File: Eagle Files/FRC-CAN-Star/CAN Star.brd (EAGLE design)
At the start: 51.5 x 30.7 mm, 12 parts

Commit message: Updated Eagle Files
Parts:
- added JUMPER1, JUMPER2: (no value), SparkFun-Connectors:1X03
- moved CAN-R1 2.27 mm to (5.59, 17.5), turned to 186 degrees
- moved CAN-R2 2.27 mm to (45.9, 17.5), turned to 174 degrees
- moved CAN-0 1.27 mm to (5.41, 3.89)
- moved CAN-1 1.27 mm to (15.6, 3.89)
- moved CAN-2 1.27 mm to (25.7, 3.89)
- moved CAN-3 1.27 mm to (35.9, 3.89)
- moved CAN-4 1.27 mm to (46.1, 3.89)
- moved CAN-5 1.27 mm to (5.41, 26.8)
- moved CAN-6 1.27 mm to (15.6, 26.8)
- moved CAN-7 1.27 mm to (25.7, 26.8)
- moved CAN-8 1.27 mm to (35.9, 26.8)
- moved CAN-9 1.27 mm to (46.1, 26.8)
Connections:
- new net N$1: CAN-R1.1, JUMPER1.1
- new net N$2: CAN-R2.1, JUMPER2.1
- net CAN-A: now also JUMPER1.2, JUMPER2.2; no longer CAN-R1.1, CAN-R2.1
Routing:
- net CAN-A: track 125.6 -> 154.0 mm
- net CAN-B: track 125.6 -> 140.1 mm
- net N$1: track 0.00 -> 11.4 mm
- net N$2: track 0.00 -> 5.55 mm
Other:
- board size 51.5 x 30.7 mm -> 53.5 x 55.1 mm
- board text added: "G(L)"
- board text added: "ON"
- board text added: "Star Board v3"
- board text added: "Y(H)"
- board text removed: "Star Board v1"

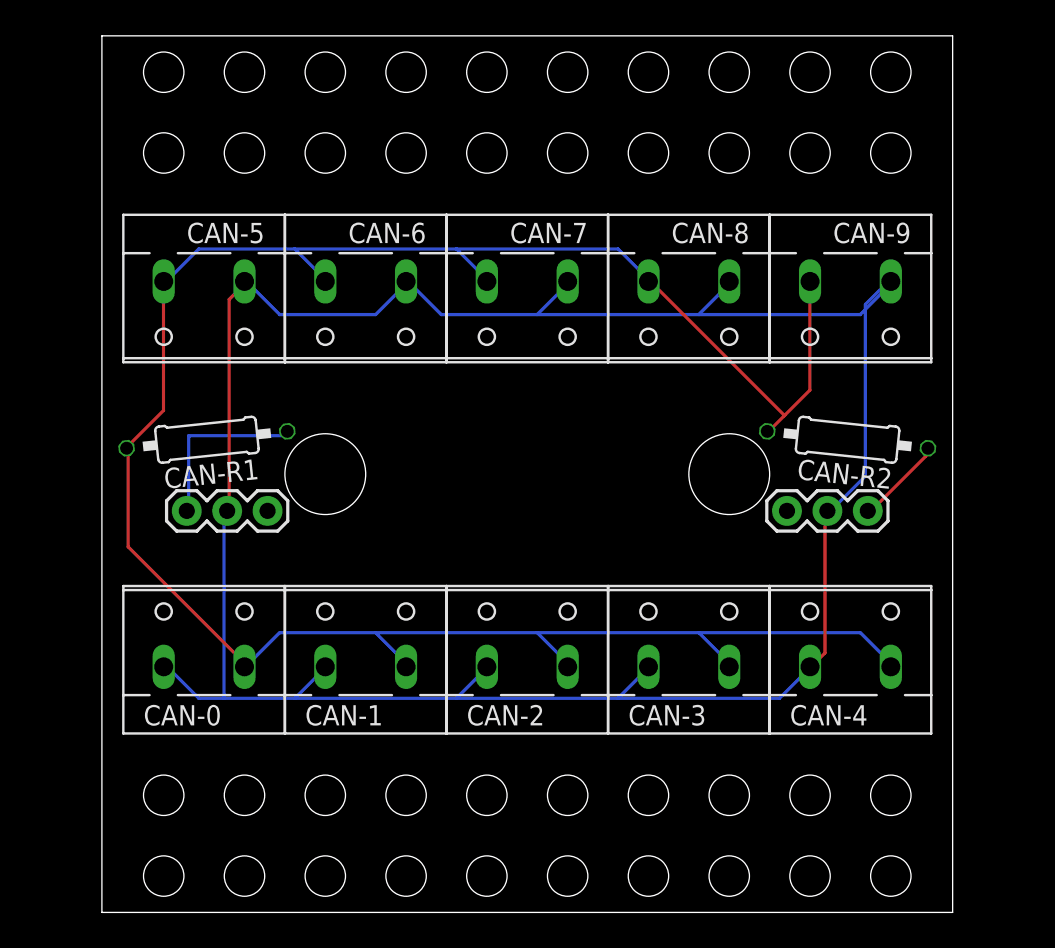
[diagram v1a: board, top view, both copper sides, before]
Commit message: Updated with strain relief holes, but not finalized yet.
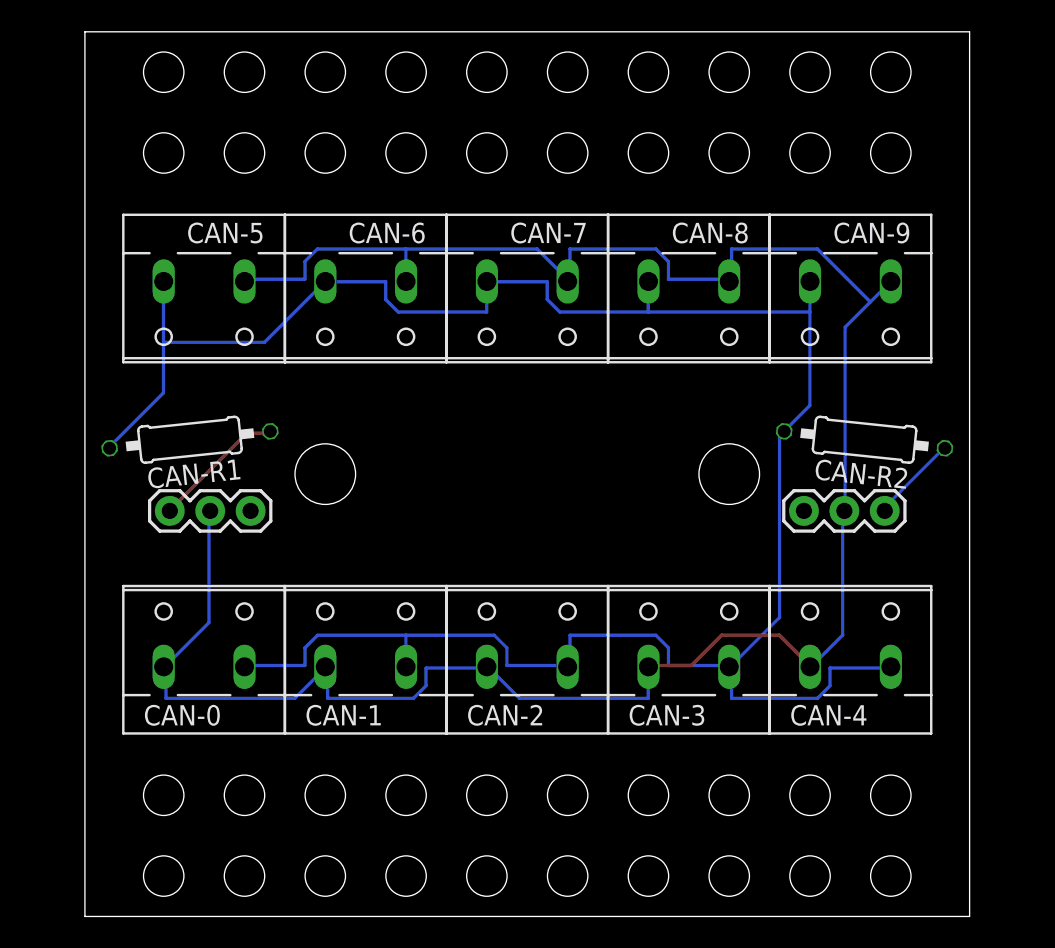
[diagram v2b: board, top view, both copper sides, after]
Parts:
- moved CAN-R2 1.07 mm to (46.9, 17.5)
- moved JUMPER1 1.07 mm to (3.25, 13.1)
- moved JUMPER2 1.07 mm to (48.2, 13.1)
- moved CAN-R1 1.07 mm to (4.52, 17.5)
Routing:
- net CAN-A: track 154.0 -> 139.4 mm
- net N$1: track 11.4 -> 8.44 mm
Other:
- board size 53.5 x 55.1 mm -> 55.6 x 55.6 mm
- board text added: "Star Board v4"
- board text removed: "Star Board v3"

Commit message: Finalized Star PCB
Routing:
- net CAN-A: track 139.4 -> 150.3 mm
- net CAN-B: track 139.7 -> 146.8 mm
- net N$1: track 8.44 -> 11.1 mm
- net N$2: track 5.53 -> 6.24 mm
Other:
- board size 55.6 x 55.6 mm -> 55.6 x 55.1 mm
- board text added: "Star Board v5"
- board text removed: "Star Board v4"

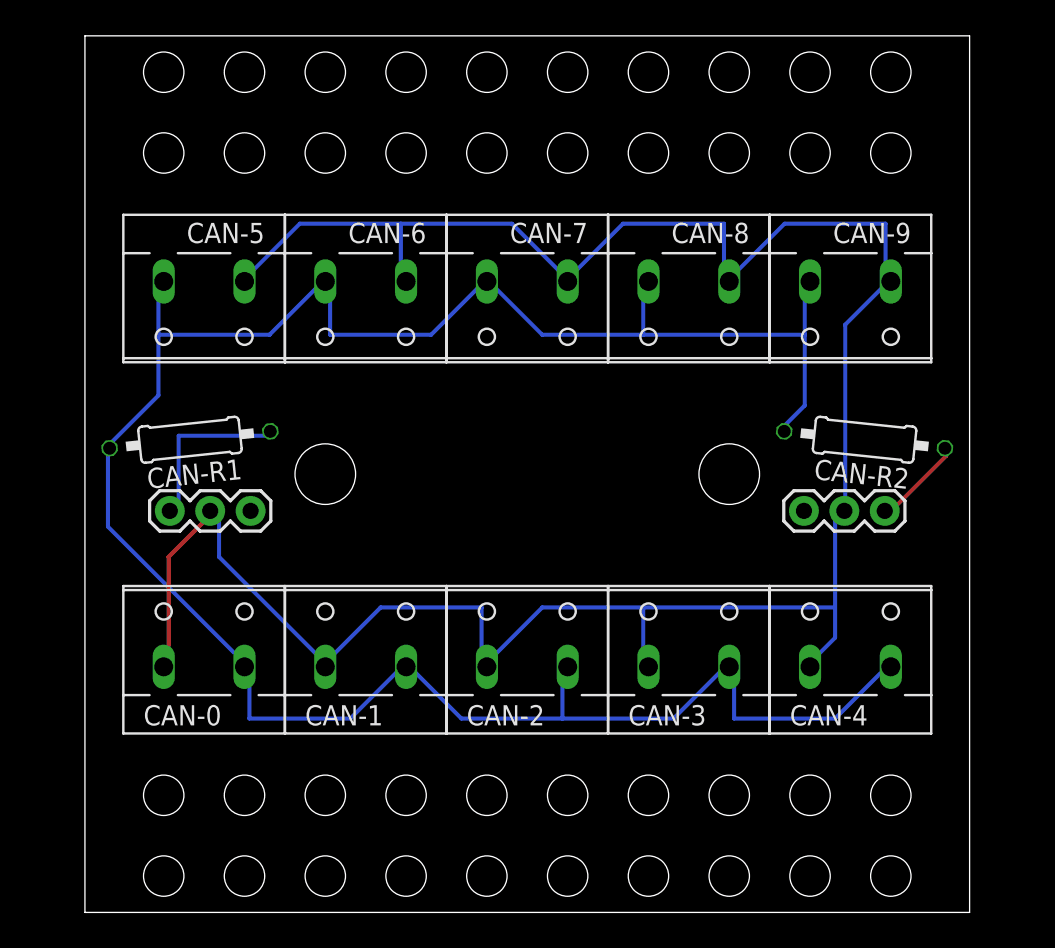
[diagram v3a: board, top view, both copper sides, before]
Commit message: Added additional mounting holes
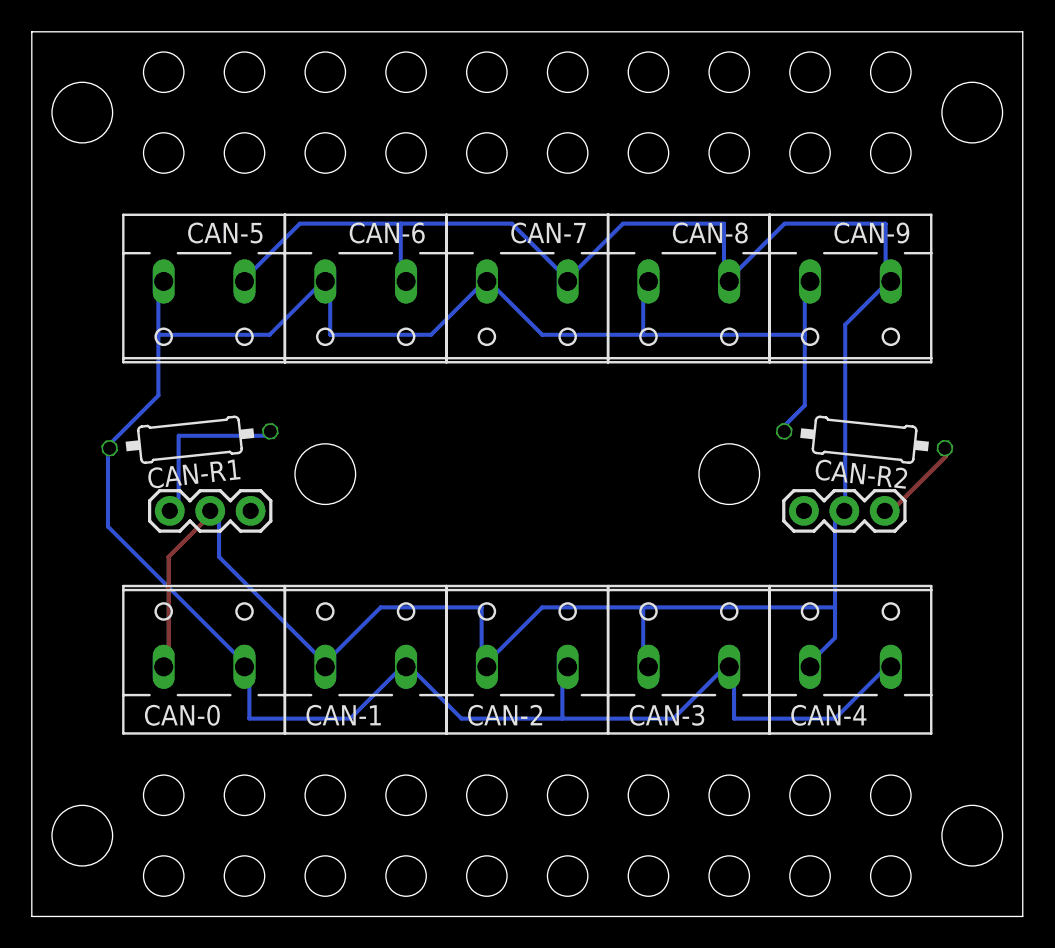
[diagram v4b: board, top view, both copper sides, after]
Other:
- board size 55.6 x 55.1 mm -> 62.3 x 55.6 mm
- board text added: "RoboLoCo Team 5338"
- board text removed: "RoboLoCo team5338.org"
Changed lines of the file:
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@@
 <layer number="18" name="Vias" color="2" fill="1" visible="yes" active="yes"/>
 <layer number="19" name="Unrouted" color="6" fill="1" visible="yes" active="yes"/>
-<layer number="20" name="Dimension" color="24" fill="1" visible="yes" active="yes"/>
+<layer number="20" name="Dimension" color="24" fill="1" visible="no" active="yes"/>
 <layer number="21" name="tPlace" color="7" fill="1" visible="yes" active="yes"/>
 <layer number="22" name="bPlace" color="7" fill="1" visible="no" active="yes"/>
-<layer number="23" name="tOrigins" color="15" fill="1" visible="yes" active="yes"/>
+<layer number="23" name="tOrigins" color="15" fill="1" visible="no" active="yes"/>
 <layer number="24" name="bOrigins" color="15" fill="1" visible="no" active="yes"/>
 <layer number="25" name="tNames" color="7" fill="1" visible="yes" active="yes"/>
@@
 <layer number="42" name="bRestrict" color="1" fill="10" visible="yes" active="yes"/>
 <layer number="43" name="vRestrict" color="2" fill="10" visible="yes" active="yes"/>
-<layer number="44" name="Drills" color="7" fill="1" visible="yes" active="yes"/>
-<layer number="45" name="Holes" color="7" fill="1" visible="yes" active="yes"/>
+<layer number="44" name="Drills" color="7" fill="1" visible="no" active="yes"/>
+<layer number="45" name="Holes" color="7" fill="1" visible="no" active="yes"/>
 <layer number="46" name="Milling" color="3" fill="1" visible="no" active="yes"/>
 <layer number="47" name="Measures" color="7" fill="1" visible="no" active="yes"/>
@@
 <board>
 <plain>
-<wire x1="-2.0828" y1="-12.192" x2="53.5432" y2="-12.192" width="0" layer="20"/>
-<wire x1="53.5432" y1="-12.192" x2="53.5432" y2="42.926" width="0" layer="20"/>
-<wire x1="53.5432" y1="42.926" x2="-2.0828" y2="42.926" width="0" layer="20"/>
-<wire x1="-2.0828" y1="42.926" x2="-2.0828" y2="-12.192" width="0" layer="20"/>
+<wire x1="-5.42416875" y1="-12.446" x2="56.88456875" y2="-12.446" width="0" layer="20"/>
+<wire x1="56.88456875" y1="-12.446" x2="56.88456875" y2="43.18" width="0" layer="20"/>
+<wire x1="56.88456875" y1="43.18" x2="-5.42416875" y2="43.18" width="0" layer="20"/>
+<wire x1="-5.42416875" y1="43.18" x2="-5.42416875" y2="-12.446" width="0" layer="20"/>
 <hole x="13.0302" y="15.367" drill="3.81" locked="yes"/>
 <hole x="38.4302" y="15.367" drill="3.81" locked="yes"/>
 <text x="25.7302" y="16.2814" size="1.651" layer="27" font="vector" ratio="10" align="center">RoboLoCo
-team5338.org</text>
+Team 5338</text>
 <text x="25.7302" y="12.954" size="1.524" layer="27" font="vector" ratio="10" align="center">Star Board v5</text>
 <text x="2.8702" y="19.939" size="1.27" layer="27" font="vector" ratio="10" align="center">Y(H)</text>
@@
 <text x="0.737615625" y="13.0556" size="1.27" layer="27" font="vector" ratio="10" align="center">ON</text>
 <text x="51.0032" y="13.0556" size="1.27" layer="27" font="vector" ratio="10" align="center">ON</text>
+<hole x="-2.249425" y="38.1" drill="3.81"/>
+<hole x="-2.249425" y="-7.366" drill="3.81"/>
+<hole x="53.709825" y="38.1" drill="3.81"/>
+<hole x="53.709825" y="-7.366" drill="3.81"/>
 </plain>
 <attributes>
